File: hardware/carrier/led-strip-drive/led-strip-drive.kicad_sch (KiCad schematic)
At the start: 5 parts

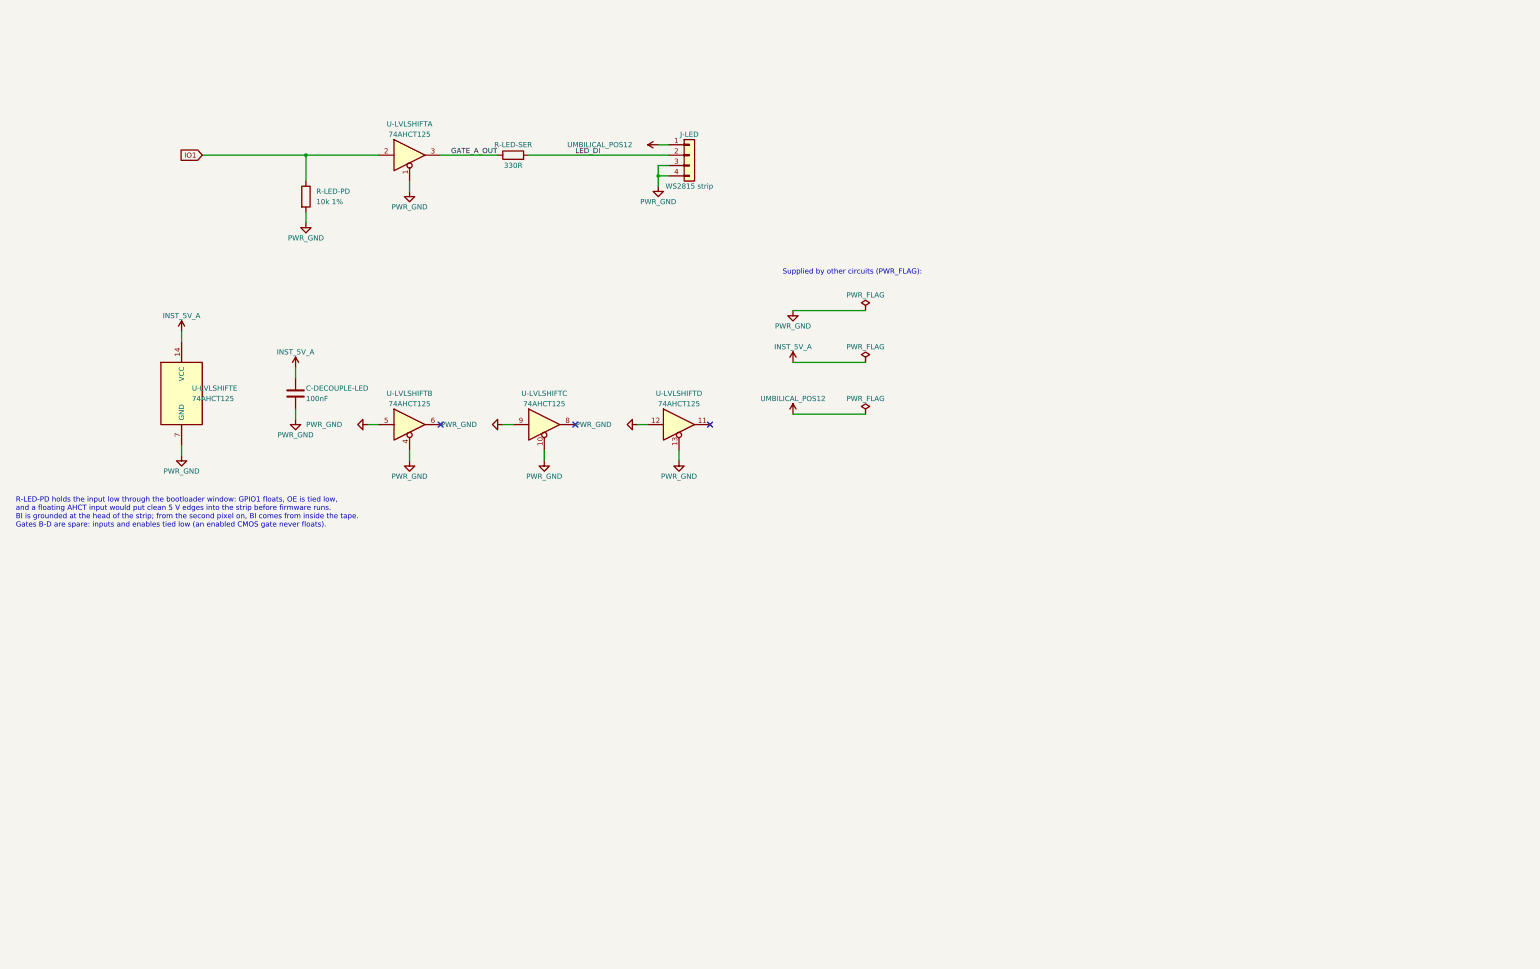
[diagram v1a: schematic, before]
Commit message: Main board in KiCad: carrier circuits migrated, main-board project placing them (ADR 0019)
- The six carrier circuits (carrier, breath-adc, breath-excitation-reference,
  power-entry-instrument, service-uart, led-strip-drive) are KiCad sources now:
  first sheets written by tools/sch.py from their netlists, each proved pin by
  pin, and each export compared part by part and net by net with the
  hand-written netlist before replacing it. Every comment of those netlists
  is carried onto its sheet as text. Pin maps cite the banked datasheets.
- Changed on purpose, before migrating: the OPA2197 is one part (U-BUF) with
  its supply pins netlisted, not two halves with the supply as metadata; the
  REF5050's unused pins are netlisted as no-connects; the two single-point
  ground joins that were "copper, not a part" are KiCad net ties (NT-AGND at
  the analog star, NT-DIG at J-UMB pin 8), the only way a board can make that
  join there and nowhere else - BOM rows, Assembly none.
- hardware/boards/main-board: the root sheet places the six circuits, both
  thumb registers, a key network per thumb key and per reserved spare (sw+,
  sw-), and a pull-up per free bit, and draws the interface circuits'
  main-board parts (J-CHAIN x2, chain series resistors, terminator, beads,
  clamp; the breath sensor with its series pair and ESD diodes; J-UMB).
  Numeric references. KiCad ERC over the hierarchy: 0 errors, 0 warnings.
- tools/kicad.py check holds the main board's J-CHAIN headers to the loom's
  J-CHAIN-MAIN (identified by rail pin) and its registers to allocation.yaml.
- README for the board with the reference table and what the layout must
  still settle; ADR 0019, tooling.md, repo-maintenance.md, CLAUDE.md follow.
- Key boards' renders and fab/ re-rendered: the shared cluster sheets gained
  the main board's instances (Gerbers differ only in timestamps).

Co-Authored-By: Claude Opus 5.5 <noreply@anthropic.com>
Claude-Session: https://claude.ai/code/session_01LmB4muFXnoLprWX4J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
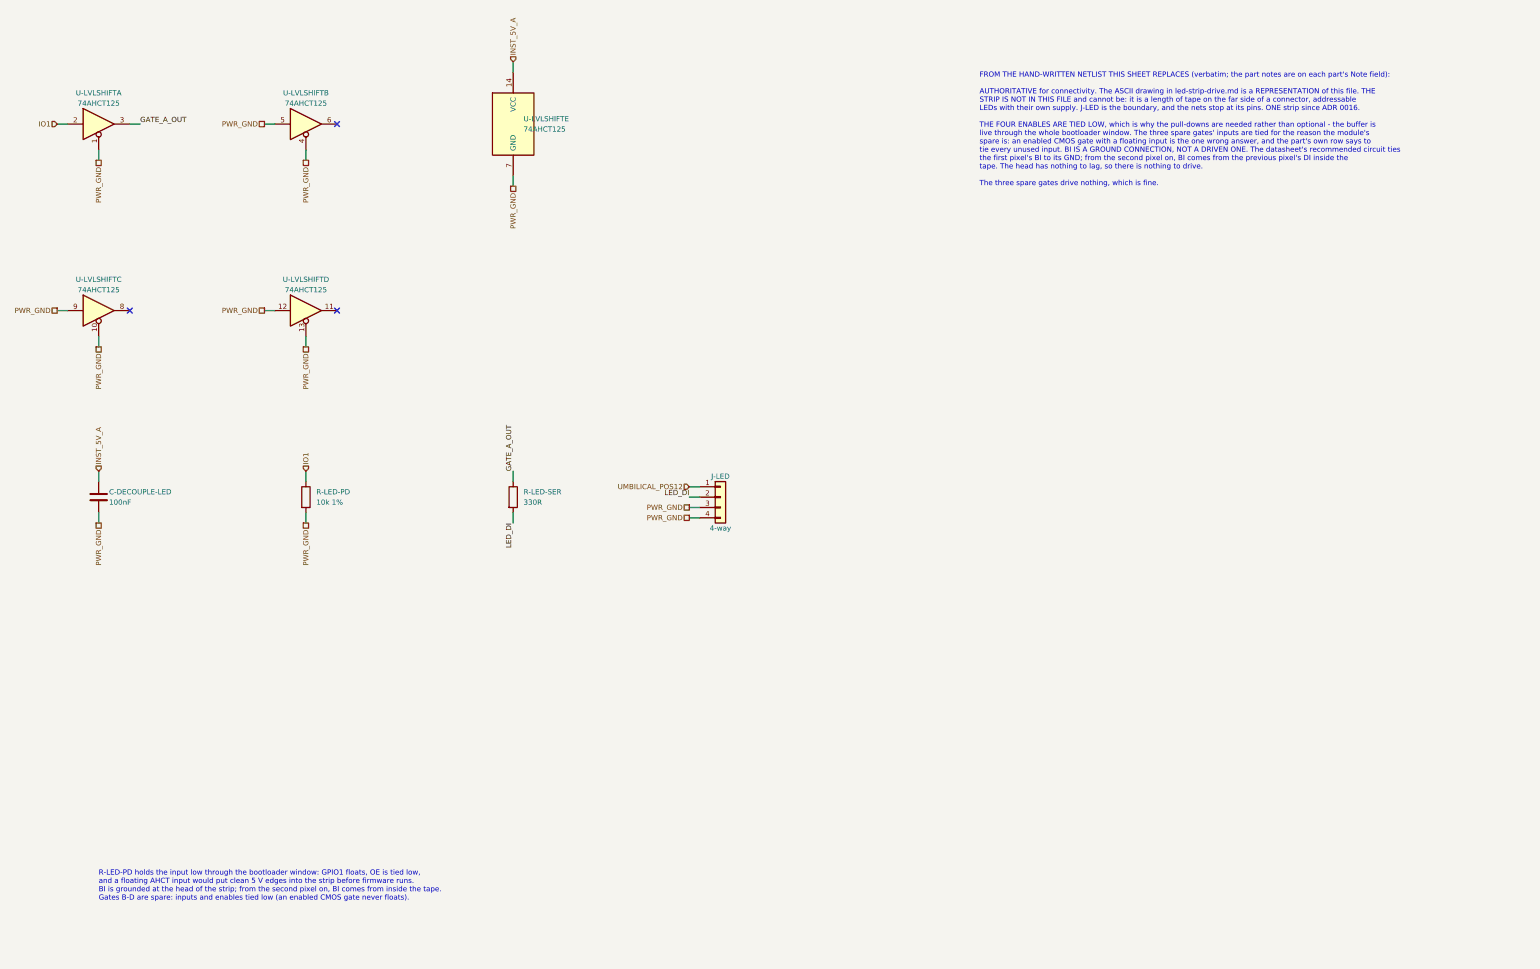
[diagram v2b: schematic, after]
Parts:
- C-DECOUPLE-LED: Drawn_as (none) -> C-DECOUPLE-CARRIER; Note (none) -> AT the package, not near it; Pins (none) -> 1=1 2=2; Row (none) -> C-DECOUPLE-CARRIER
- J-LED: value WS2815 strip -> 4-way; Note (none) -> Strip power passes through this connector and is carrier/po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; Pins (none) -> POS12=1 GND=4 DI=2 BI=3; Pins_source (none) -> supply and ground at the ends, the two data lines together,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; Row (none) -> J-LED
- R-LED-PD: Note (none) -> PULL-DOWN, and it cannot be added later. GPIO1 is high-impe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; Pins (none) -> 1=1 2=2; Row (none) -> R-LED-PD
- R-LED-SER: Note (none) -> Series into the strip's DI, the vendor's recommended circuit; Pins (none) -> 1=1 2=2; Row (none) -> R-LED-SER
- U-LVLSHIFT: Note (none) -> ON THE 5 V RAIL, and that is the point: TTL thresholds mean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; Pins (none) -> 1A=2 1Y=3 1OE=1 2A=5 2Y=6 2OE=4 3A=9 3Y=8 3OE=10 4A=12 4Y=1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; Pins_source (none) -> datasheets/logic/SN74AHCT125.pdf p.1 pin-out (SOIC-14): 1OE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; Row (none) -> U-LVLSHIFT
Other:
- note added: "FROM THE HAND-WRITTEN NETLIST THIS SHEET REPLACES (verbatim; the part notes are on each part's Note field): AUTHORITATIVE for connectivity. The ASCII drawing in led-strip-drive.md is a REPRESENTATION of this file. THE STRIP IS NOT IN THIS FILE and cannot be: it is a length of tape on the far side of a connector, addressable LEDs with their own supply. J-LED is the boundary, and the nets stop at i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"
- note removed: "Supplied by other circuits (PWR_FLAG):"
- title: LED strip drive (carrier/led-strip-drive) -> LED strip drive (hardware/carrier/led-strip-drive)
- moved on the sheet: C-DECOUPLE-LED, J-LED, R-LED-PD, R-LED-SER, U-LVLSHIFTA, U-LVLSHIFTB, U-LVLSHIFTC, U-LVLSHIFTD, U-LVLSHIFTE

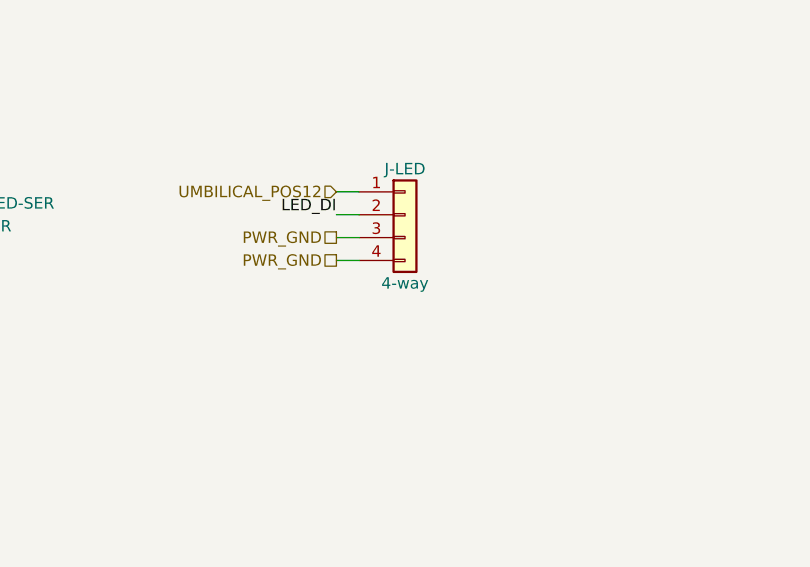
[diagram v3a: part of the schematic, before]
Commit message: Main board: apply the chosen parts to every symbol and row
Every main-board and adapter symbol now carries Footprint, Manufacturer,
MPN, LCSC and Assembly. The values come from the selections whose
datasheets are banked. The BOM rows follow those choices:

- D-USBOR is the SS14 (SMA).
- J-LED is four solder pads, not a connector.
- L-BUCK-IN is 22 uH, C-BUCK-IN is a UCM electrolytic, C-STRIP-BULK is
  470 uF 25 V.
- D-TVS-BREATH is the PESD12VS1UA (SOD-323); the UB is SOD523.
- J-UMB is the hanxia header. Its posts go through the adapter and its
  tails through the tongue; the old wording had them swapped.
- U-BUCK and U-BREATH say where to buy.
- C-ADC-BULK is 1206 if fitted.

The body and geometry follow the chosen parts:

- The J-UMB and J-MCU envelopes in config/body.yaml are now read off the
  parts' drawings.
- J-MCU is longer, so the regulator block moved and the right-hand ribbon
  header followed it by 1.5 mm. The RH key board is re-laid out, with C8
  moving with the header's 3V3 pin. It checks clean.
- A mount candidate is now nudged by up to 3 mm before it is dropped. All
  seven main-board mounts hold.

New footprints and pages:

- New woody.pretty footprints: the MPXV4006DP (case 1351-01) from
  breath-sense-link.md's land pattern, and the NE8FAV from Neutrik's
  layout, mirrored to the top view.
- The input-LC derivation uses the chosen capacitor's banked ESR: Q is at
  most 1.8, and the margin is 120x worst case.
- The main-board README lists what is still open before layout.

Co-Authored-By: Claude Opus 5.5 <noreply@anthropic.com>
Claude-Session: https://claude.ai/code/session_01LmB4muFXnoLprWX4JzuJ5A
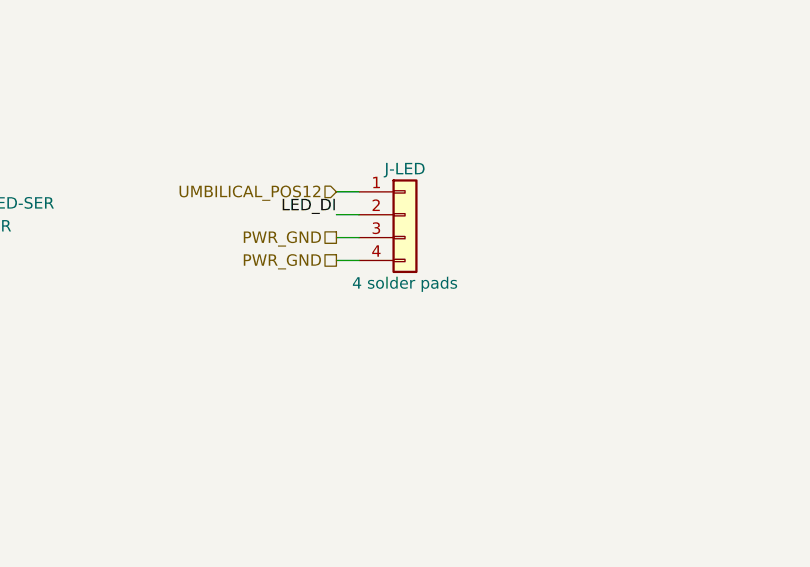
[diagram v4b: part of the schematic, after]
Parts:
- C-DECOUPLE-LED: footprint (none) -> Capacitor_SMD:C_0805_2012Metric; Assembly (none) -> machine; LCSC (none) -> C49678; MPN (none) -> CC0805KRX7R9BB104; Manufacturer (none) -> YAGEO
- J-LED: value 4-way -> 4 solder pads; footprint (none) -> Connector_PinHeader_2.54mm:PinHeader_1x04_P2.54mm_Vertical; Assembly (none) -> none; Note Strip power passes through this connector and is carrier/po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 -> Four solder pads, no connector (BOM row J-LED): the strip's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; Pins_source supply and ground at the ends, the two data lines together,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 -> pads in the silkscreen's order: 1 12V, 2 DI, 3 BI, 4 GND - 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
- R-LED-PD: footprint (none) -> Resistor_SMD:R_0805_2012Metric; Assembly (none) -> machine; LCSC (none) -> C17414; MPN (none) -> 0805W8F1002T5E; Manufacturer (none) -> UNI-ROYAL
- R-LED-SER: footprint (none) -> Resistor_SMD:R_0805_2012Metric; Assembly (none) -> machine; LCSC (none) -> C17630; MPN (none) -> 0805W8F3300T5E; Manufacturer (none) -> UNI-ROYAL
- U-LVLSHIFT: footprint (none) -> Package_SO:SOIC-14_3.9x8.7mm_P1.27mm; Assembly (none) -> machine; LCSC (none) -> C155176; MPN (none) -> SN74AHCT125DR; Manufacturer (none) -> Texas Instruments
